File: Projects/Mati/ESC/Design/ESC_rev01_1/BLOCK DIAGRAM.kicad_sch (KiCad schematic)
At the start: 0 parts

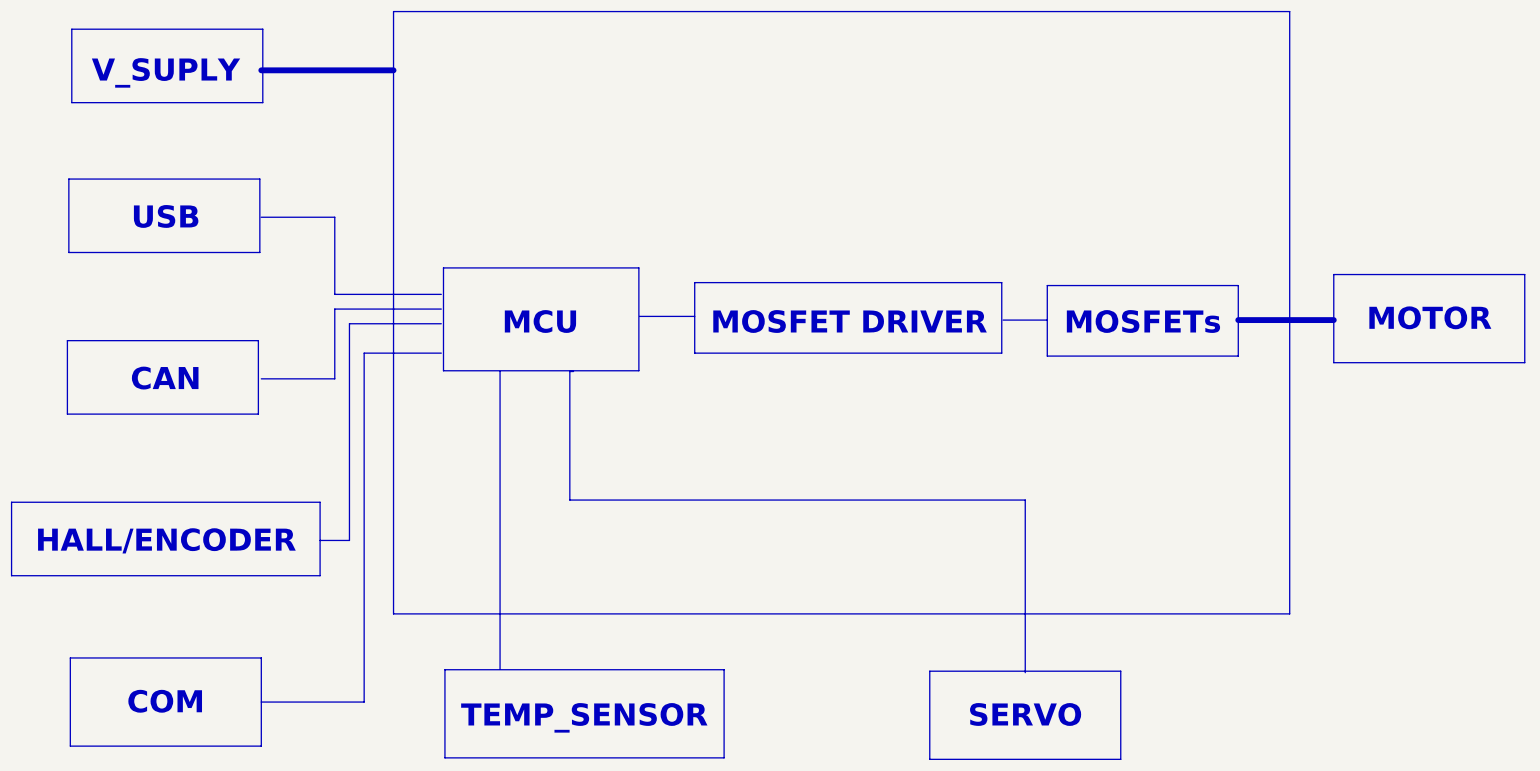
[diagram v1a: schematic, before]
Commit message: Update 05
Transistors & ESC Motor Phases Schematics
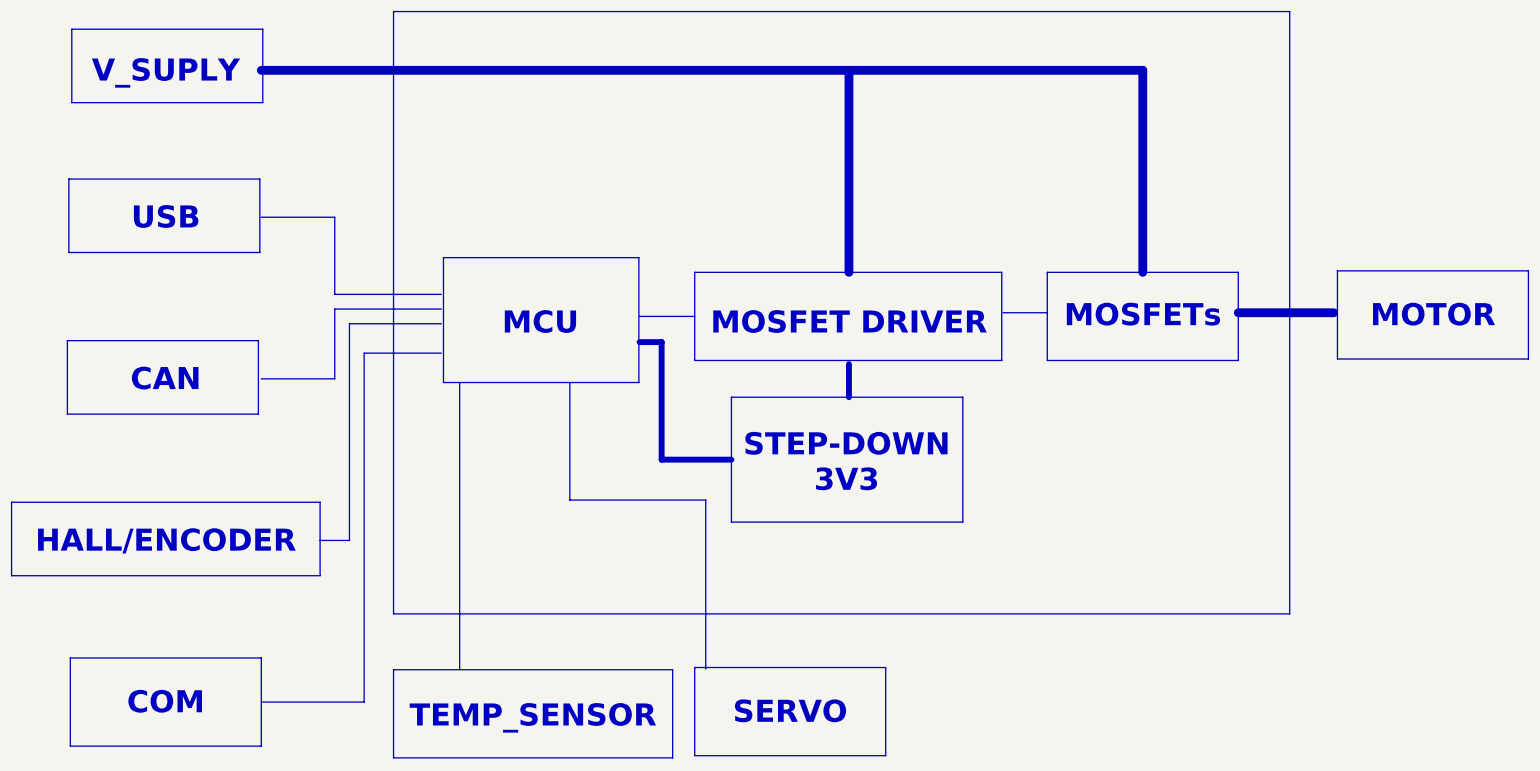
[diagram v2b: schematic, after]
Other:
- note added: "STEP-DOWN 3V3"
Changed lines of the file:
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@@
 	(polyline
 		(pts
-			(xy 229.87 86.36) (xy 246.38 86.36)
+			(xy 130.175 110.49) (xy 130.175 90.17)
 		)
 		(stroke
@@
 	(polyline
 		(pts
+			(xy 229.87 85.09) (xy 246.38 85.09)
+		)
+		(stroke
+			(width 1.524)
+			(type default)
+		)
+	)
+	(polyline
+		(pts
 			(xy 73.66 81.915) (xy 92.075 81.915)
 		)
@@
 	(polyline
 		(pts
-			(xy 114.3 117.475) (xy 114.3 95.25)
-		)
-		(stroke
-			(width 0)
-			(type default)
-		)
-	)
-	(polyline
-		(pts
-			(xy 189.23 86.36) (xy 196.85 86.36)
-		)
-		(stroke
-			(width 0)
-			(type default)
-		)
-	)
-	(polyline
-		(pts
-			(xy 102.235 95.25) (xy 102.235 146.685)
+			(xy 162.56 99.695) (xy 162.56 93.98)
+		)
+		(stroke
+			(width 1.016)
+			(type default)
+		)
+	)
+	(polyline
+		(pts
+			(xy 114.3 117.475) (xy 114.3 97.155)
+		)
+		(stroke
+			(width 0)
+			(type default)
+		)
+	)
+	(polyline
+		(pts
+			(xy 189.23 85.09) (xy 196.85 85.09)
+		)
+		(stroke
+			(width 0)
+			(type default)
+		)
+	)
+	(polyline
+		(pts
+			(xy 95.25 97.155) (xy 95.25 146.685)
 		)
 		(stroke
@@
 	(polyline
 		(pts
-			(xy 60.96 43.18) (xy 83.82 43.18)
+			(xy 213.36 78.105) (xy 213.36 43.18)
+		)
+		(stroke
+			(width 1.524)
+			(type default)
+		)
+	)
+	(polyline
+		(pts
+			(xy 162.56 78.105) (xy 162.56 43.18)
+		)
+		(stroke
+			(width 1.524)
+			(type default)
+		)
+	)
+	(polyline
+		(pts
+			(xy 60.96 43.18) (xy 213.36 43.18)
+		)
+		(stroke
+			(width 1.524)
+			(type default)
+		)
+	)
+	(polyline
+		(pts
+			(xy 73.66 96.52) (xy 73.66 84.455)
+		)
+		(stroke
+			(width 0)
+			(type default)
+		)
+	)
+	(polyline
+		(pts
+			(xy 137.795 117.475) (xy 114.3 117.475)
+		)
+		(stroke
+			(width 0)
+			(type default)
+		)
+	)
+	(polyline
+		(pts
+			(xy 137.795 146.685) (xy 137.795 117.475)
+		)
+		(stroke
+			(width 0)
+			(type default)
+		)
+	)
+	(polyline
+		(pts
+			(xy 60.96 68.58) (xy 73.66 68.58)
+		)
+		(stroke
+			(width 0)
+			(type default)
+		)
+	)
+	(polyline
+		(pts
+			(xy 142.24 110.49) (xy 130.175 110.49)
 		)
 		(stroke
@@
 	(polyline
 		(pts
-			(xy 73.66 96.52) (xy 73.66 84.455)
-		)
-		(stroke
-			(width 0)
-			(type default)
-		)
-	)
-	(polyline
-		(pts
-			(xy 193.04 117.475) (xy 114.3 117.475)
-		)
-		(stroke
-			(width 0)
-			(type default)
-		)
-	)
-	(polyline
-		(pts
-			(xy 114.3 95.25) (xy 114.935 95.25)
-		)
-		(stroke
-			(width 0)
-			(type default)
-		)
-	)
-	(polyline
-		(pts
-			(xy 193.04 147.32) (xy 193.04 117.475)
-		)
-		(stroke
-			(width 0)
-			(type default)
-		)
-	)
-	(polyline
-		(pts
-			(xy 60.96 68.58) (xy 73.66 68.58)
-		)
-		(stroke
-			(width 0)
-			(type default)
-		)
-	)
-	(polyline
-		(pts
 			(xy 126.365 85.725) (xy 135.89 85.725)
 		)
@@
 		(stroke
 			(width 0)
+			(type default)
+		)
+	)
+	(polyline
+		(pts
+			(xy 130.175 90.17) (xy 126.365 90.17)
+		)
+		(stroke
+			(width 1.016)
 			(type default)
 		)
@@
 	)
 	(rectangle
+		(start 142.24 99.695)
+		(end 182.245 121.285)
+		(stroke
+			(width 0)
+			(type default)
+		)
+		(fill
+			(type none)
+		)
+	)
+	(rectangle
 		(start 28.194 36.068)
 		(end 61.214 48.768)
@@
 	)
 	(rectangle
-		(start 92.456 77.343)
-		(end 126.238 95.123)
-		(stroke
-			(width 0)
-			(type default)
-		)
-		(fill
-			(type none)
-		)
-	)
-	(rectangle
-		(start 196.85 80.391)
-		(end 229.87 92.583)
-		(stroke
-			(width 0)
-			(type default)
-		)
-		(fill
-			(type none)
-		)
-	)
-	(rectangle
-		(start 92.71 146.812)
-		(end 140.97 162.052)
+		(start 92.456 75.565)
+		(end 126.238 97.155)
+		(stroke
+			(width 0)
+			(type default)
+		)
+		(fill
+			(type none)
+		)
+	)
+	(rectangle
+		(start 196.85 78.105)
+		(end 229.87 93.345)
+		(stroke
+			(width 0)
+			(type default)
+		)
+		(fill
+			(type none)
+		)
+	)
+	(rectangle
+		(start 83.82 146.812)
+		(end 132.08 162.052)
 		(stroke
 			(width 0)
@@
 	)
 	(rectangle
-		(start 176.53 147.066)
-		(end 209.55 162.306)
+		(start 135.89 146.431)
+		(end 168.91 161.671)
 		(stroke
 			(width 0)
@@
 	)
 	(rectangle
-		(start 135.89 79.883)
-		(end 188.976 92.075)
+		(start 135.89 78.105)
+		(end 188.976 93.345)
 		(stroke
 			(width 0)
@@
 	)
 	(rectangle
-		(start 246.38 78.486)
-		(end 279.4 93.726)
+		(start 247.015 77.851)
+		(end 280.035 93.091)
 		(stroke
 			(width 0)
@@
 	(text "TEMP_SENSOR"
 		(exclude_from_sim no)
-		(at 116.84 154.94 0)
+		(at 107.95 154.94 0)
 		(effects
 			(font
@@
 	(text "SERVO"
 		(exclude_from_sim no)
-		(at 193.04 154.94 0)
+		(at 152.4 154.305 0)
 		(effects
 			(font
@@
 	(text "MOSFETs"
 		(exclude_from_sim no)
-		(at 213.36 86.995 0)
+		(at 213.36 85.725 0)
 		(effects
 			(font
@@
 		)
 	)
+	(text "STEP-DOWN\n3V3"
+		(exclude_from_sim no)
+		(at 162.179 111.125 0)
+		(effects
+			(font
+				(size 3.81 3.81)
+				(thickness 1.016)
+				(bold yes)
+			)
+		)
+	)
 	(text "V_SUPLY"
 		(exclude_from_sim no)
@@
 	(text "MOTOR"
 		(exclude_from_sim no)
-		(at 262.89 86.36 0)
-		(effects
-			(font
+		(at 263.525 85.725 0)
+		(effects
+			(font

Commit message: Update 06
USB, CAN Bus, TVS, and Schematic Completion
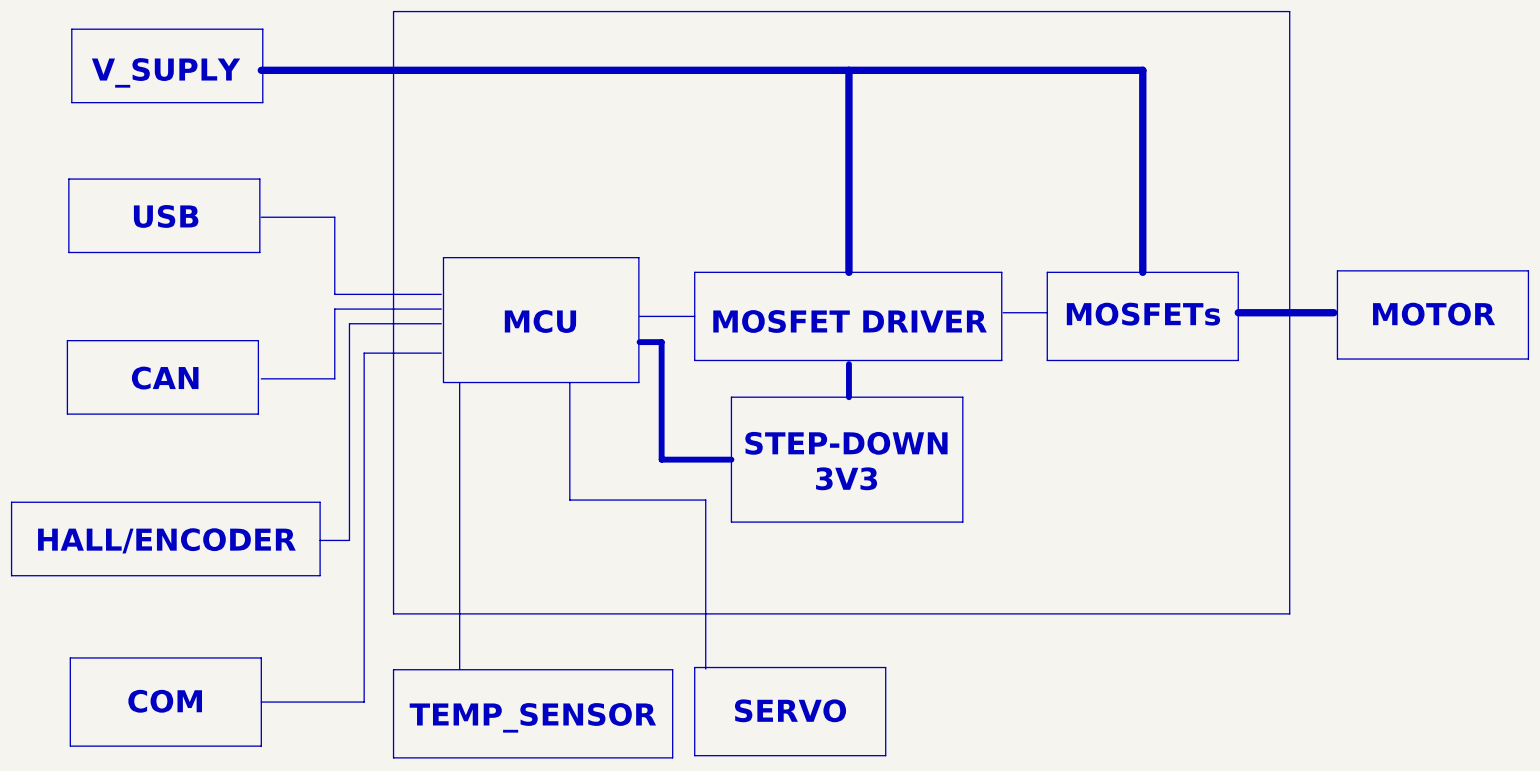
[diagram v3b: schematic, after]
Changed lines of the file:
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@@
 		)
 		(stroke
-			(width 1.524)
+			(width 1.27)
 			(type default)
 		)
@@
 		)
 		(stroke
-			(width 1.524)
+			(width 1.27)
 			(type default)
 		)
@@
 		)
 		(stroke
-			(width 1.524)
+			(width 1.27)
 			(type default)
 		)
@@
 		)
 		(stroke
-			(width 1.524)
+			(width 1.27)
 			(type default)
 		)
